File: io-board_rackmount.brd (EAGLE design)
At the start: 124 x 90.3 mm, 12 parts, among them X1 22-23-2041, X3 22-23-2101

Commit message: Minor fixes
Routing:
- net DGND: track 54.8 -> 56.6 mm
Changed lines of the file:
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@@
 </class>
 </classes>
-<designrules name="default">
+<designrules name="default *">
 <description language="de">&lt;b&gt;EAGLE Design Rules&lt;/b&gt;
 &lt;p&gt;
@@
 <param name="mtCopper" value="0.035mm 0.035mm 0.035mm 0.035mm 0.035mm 0.035mm 0.035mm 0.035mm 0.035mm 0.035mm 0.035mm 0.035mm 0.035mm 0.035mm 0.035mm 0.035mm"/>
 <param name="mtIsolate" value="1.5mm 0.15mm 0.2mm 0.15mm 0.2mm 0.15mm 0.2mm 0.15mm 0.2mm 0.15mm 0.2mm 0.15mm 0.2mm 0.15mm 0.2mm"/>
-<param name="mdWireWire" value="8mil"/>
-<param name="mdWirePad" value="8mil"/>
-<param name="mdWireVia" value="8mil"/>
-<param name="mdPadPad" value="8mil"/>
-<param name="mdPadVia" value="8mil"/>
-<param name="mdViaVia" value="8mil"/>
-<param name="mdSmdPad" value="8mil"/>
-<param name="mdSmdVia" value="8mil"/>
-<param name="mdSmdSmd" value="8mil"/>
+<param name="mdWireWire" value="7mil"/>
+<param name="mdWirePad" value="7mil"/>
+<param name="mdWireVia" value="7mil"/>
+<param name="mdPadPad" value="7mil"/>
+<param name="mdPadVia" value="7mil"/>
+<param name="mdViaVia" value="7mil"/>
+<param name="mdSmdPad" value="7mil"/>
+<param name="mdSmdVia" value="7mil"/>
+<param name="mdSmdSmd" value="7mil"/>
 <param name="mdViaViaSameLayer" value="8mil"/>
 <param name="mnLayersViaInSmd" value="2"/>
-<param name="mdCopperDimension" value="40mil"/>
-<param name="mdDrill" value="8mil"/>
+<param name="mdCopperDimension" value="25mil"/>
+<param name="mdDrill" value="7mil"/>
 <param name="mdSmdStop" value="0mil"/>
 <param name="msWidth" value="10mil"/>
-<param name="msDrill" value="24mil"/>
+<param name="msDrill" value="10mil"/>
 <param name="msMicroVia" value="9.99mm"/>
 <param name="msBlindViaRatio" value="0.5"/>
@@
 </polygon>
 <contactref element="CH1" pad="P$2"/>
-<wire x1="72.644" y1="4.318" x2="75.184" y2="4.318" width="0.4064" layer="16"/>
+<wire x1="72.644" y1="4.572" x2="75.184" y2="4.572" width="1.016" layer="16"/>
 <contactref element="CH2" pad="P$2"/>
 <contactref element="CH4" pad="P$2"/>
@@
 <contactref element="U$3" pad="P$8"/>
 <contactref element="U$3" pad="P$17"/>
-<wire x1="57.404" y1="9.398" x2="57.404" y2="10.922" width="0.4064" layer="16"/>
-<wire x1="56.896" y1="4.318" x2="54.864" y2="4.318" width="0.4064" layer="16"/>
+<wire x1="57.658" y1="9.398" x2="57.658" y2="10.922" width="1.016" layer="16"/>
+<wire x1="56.896" y1="4.572" x2="54.864" y2="4.572" width="1.016" layer="16"/>
 <via x="11.684" y="46.609" extent="1-16" drill="1.1"/>
 <wire x1="11.684" y1="46.609" x2="5.969" y2="46.609" width="1.6764" layer="16"/>
@@
 <via x="69.02" y="12.378" extent="1-16" drill="0.6" shape="square"/>
 <via x="61.52" y="8.584" extent="1-16" drill="0.6" shape="square"/>
+<wire x1="72.136" y1="9.398" x2="73.914" y2="9.398" width="1.016" layer="16"/>
 </signal>
 <signal name="N$23">

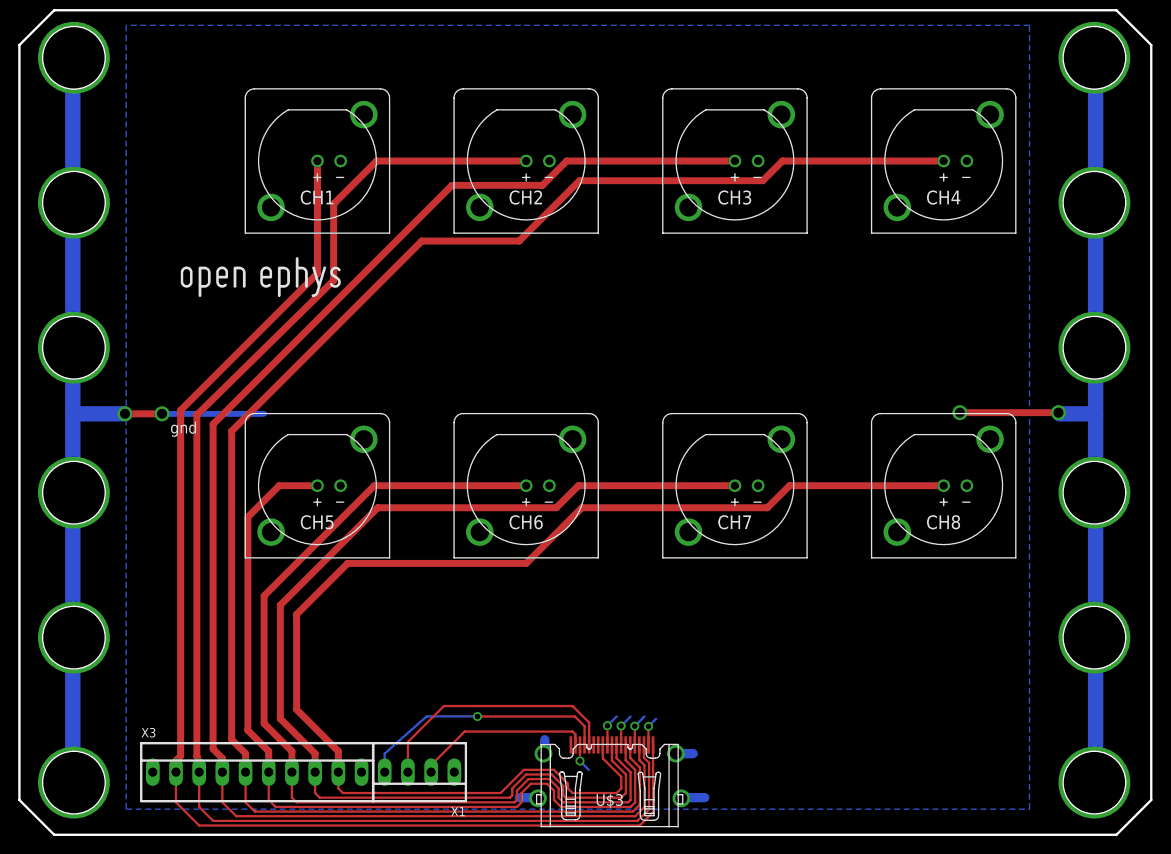
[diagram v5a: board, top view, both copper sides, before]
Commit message: hole pattern now fits 19" rack
changed spacing to 0.625, 0.625, 0.5, 0.625, 0.625
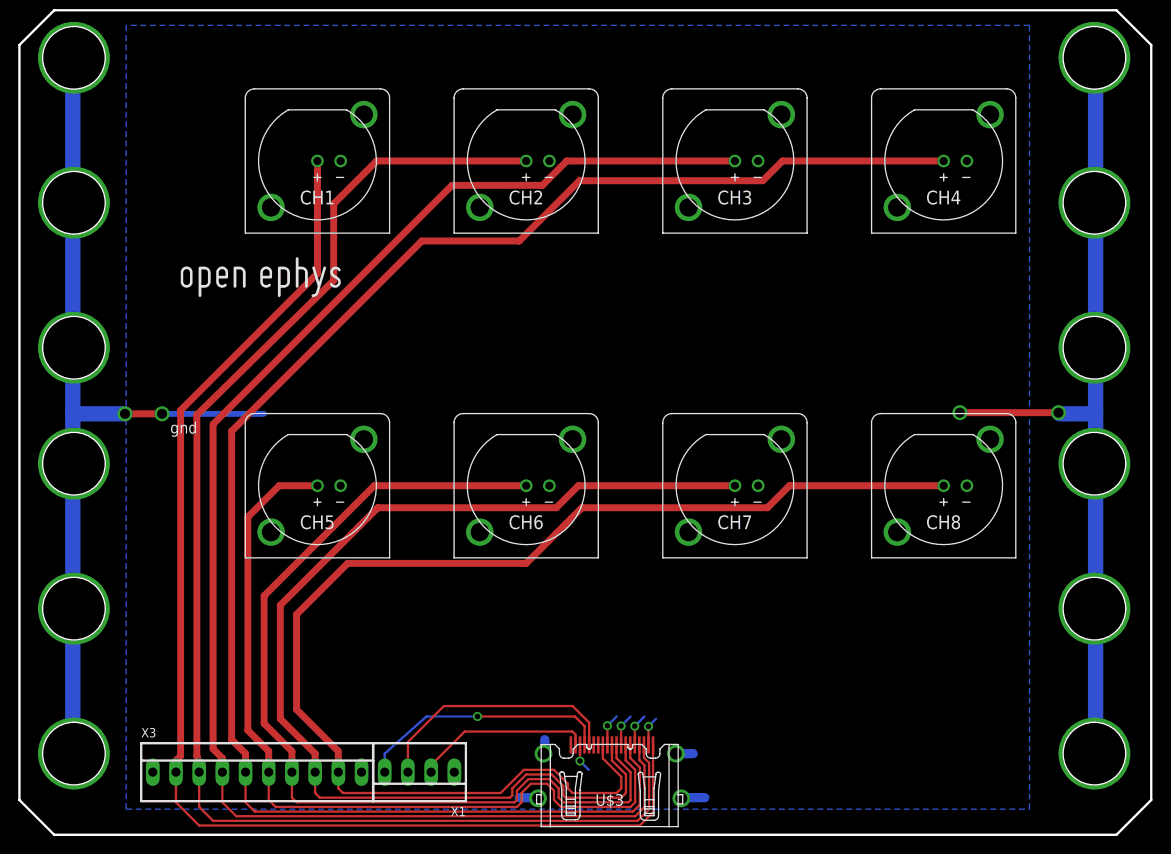
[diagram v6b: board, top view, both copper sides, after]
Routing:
- net S$14: track 79.4 -> 76.2 mm
- net S$13: track 77.1 -> 73.9 mm
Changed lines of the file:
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@@
 <?xml version="1.0" encoding="utf-8"?>
 <!DOCTYPE eagle SYSTEM "eagle.dtd">
-<eagle version="6.3">
+<eagle version="6.1">
 <drawing>
 <settings>
@@
 <setting verticaltext="up"/>
 </settings>
-<grid distance="10" unitdist="mil" unit="mil" style="lines" multiple="1" display="yes" altdistance="0.025" altunitdist="inch" altunit="inch"/>
+<grid distance="0.005" unitdist="inch" unit="inch" style="lines" multiple="1" display="yes" altdistance="0.025" altunitdist="inch" altunit="inch"/>
 <layers>
 <layer number="1" name="Top" color="4" fill="1" visible="yes" active="yes"/>
@@
 <layer number="14" name="Route14" color="1" fill="6" visible="no" active="no"/>
 <layer number="15" name="Route15" color="4" fill="6" visible="no" active="no"/>
-<layer number="16" name="Bottom" color="8" fill="1" visible="yes" active="yes"/>
+<layer number="16" name="Bottom" color="9" fill="1" visible="yes" active="yes"/>
 <layer number="17" name="Pads" color="2" fill="1" visible="yes" active="yes"/>
 <layer number="18" name="Vias" color="2" fill="1" visible="yes" active="yes"/>
@@
 <hole x="6.096" y="69.723" drill="6.858"/>
 <hole x="6.096" y="53.848" drill="6.858"/>
-<hole x="6.096" y="37.973" drill="6.858"/>
-<hole x="6.096" y="22.098" drill="6.858"/>
-<hole x="6.096" y="6.223" drill="6.858"/>
+<hole x="6.096" y="41.148" drill="6.858"/>
+<hole x="6.096" y="25.273" drill="6.858"/>
+<hole x="6.096" y="9.398" drill="6.858"/>
 <wire x1="120.269" y1="0.508" x2="3.937" y2="0.508" width="0.254" layer="20"/>
 <wire x1="3.937" y1="0.508" x2="0.127" y2="4.318" width="0.254" layer="20"/>
@@
 <hole x="117.856" y="69.723" drill="6.858"/>
 <hole x="117.856" y="53.848" drill="6.858"/>
-<hole x="117.856" y="37.973" drill="6.858"/>
-<hole x="117.856" y="22.098" drill="6.858"/>
-<hole x="117.856" y="6.223" drill="6.858"/>
+<hole x="117.856" y="41.148" drill="6.858"/>
+<hole x="117.856" y="25.273" drill="6.858"/>
+<hole x="117.856" y="9.398" drill="6.858"/>
 </plain>
 <attributes>
@@
 </class>
 </classes>
-<designrules name="default *">
+<designrules>
 <description language="de">&lt;b&gt;EAGLE Design Rules&lt;/b&gt;
 &lt;p&gt;
@@
 </signal>
 <signal name="S$4">
-<via x="6.096" y="37.973" extent="1-16" drill="6.858"/>
+<via x="6.096" y="41.148" extent="1-16" drill="6.858"/>
 </signal>
 <signal name="S$5">
-<via x="6.096" y="22.098" extent="1-16" drill="6.858"/>
+<via x="6.096" y="25.273" extent="1-16" drill="6.858"/>
 </signal>
 <signal name="S$6">
-<via x="6.096" y="6.223" extent="1-16" drill="6.858"/>
+<via x="6.096" y="9.398" extent="1-16" drill="6.858"/>
 </signal>
 <signal name="S$13">
-<wire x1="5.969" y1="84.836" x2="5.969" y2="7.747" width="1.6764" layer="16"/>
+<wire x1="5.969" y1="84.836" x2="5.969" y2="10.922" width="1.6764" layer="16"/>
 </signal>
 <signal name="VCC">
@@
 </signal>
 <signal name="S$10">
-<via x="117.856" y="37.973" extent="1-16" drill="6.858"/>
+<via x="117.856" y="41.148" extent="1-16" drill="6.858"/>
 </signal>
 <signal name="S$11">
-<via x="117.856" y="22.098" extent="1-16" drill="6.858"/>
+<via x="117.856" y="25.273" extent="1-16" drill="6.858"/>
 </signal>
 <signal name="S$12">
-<via x="117.856" y="6.223" extent="1-16" drill="6.858"/>
+<via x="117.856" y="9.398" extent="1-16" drill="6.858"/>
 </signal>
 <signal name="S$14">
-<wire x1="117.983" y1="85.09" x2="117.983" y2="5.715" width="1.6764" layer="16"/>
+<wire x1="117.983" y1="85.09" x2="117.983" y2="8.89" width="1.6764" layer="16"/>
 </signal>
 </signals>
